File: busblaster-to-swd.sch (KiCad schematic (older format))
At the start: 5 parts, among them J101 CONN_02X10, J102 Tag Connect, J103 CONN_02X05

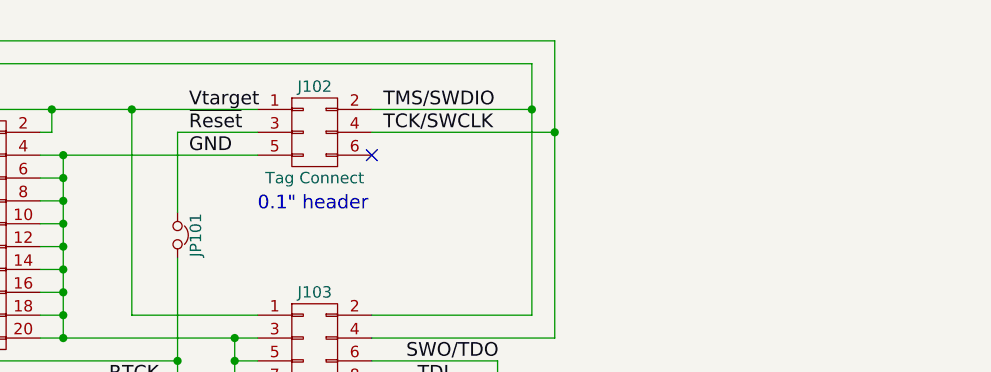
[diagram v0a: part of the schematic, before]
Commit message: Add SWCLK pullup resistor footprint
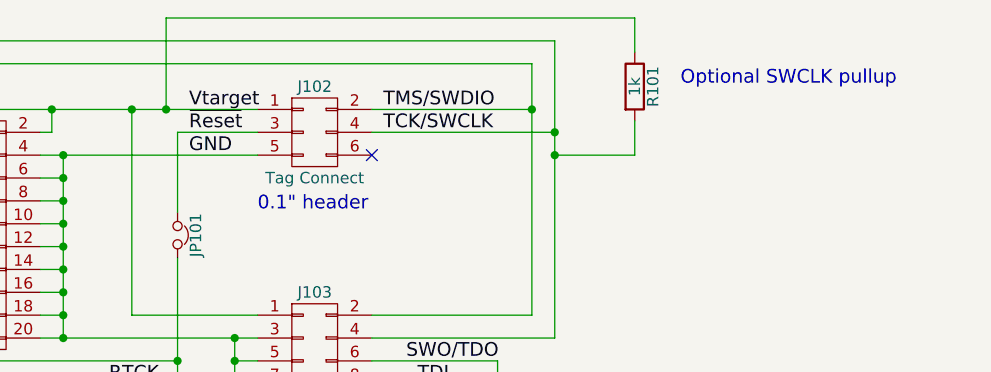
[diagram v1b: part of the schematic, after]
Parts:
- added R101: 1k, Resistors_SMD:R_0603_HandSoldering, symbol R
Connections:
- net TCK/SWCLK: now also R101.2
- net Vtarget: now also R101.1
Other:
- note added: "Optional SWCLK pullup"
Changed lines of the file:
@@
 LIBS:contrib
 LIBS:valves
+LIBS:busblaster-to-swd-cache
 EELAYER 25 0
 EELAYER END
@@
 Text Label 4200 3900 0    60   ~ 0
 RTCK
+$Comp
+L R R101
+U 1 1 590555B6
+P 6500 2600
+F 0 "R101" V 6580 2600 50  0000 C CNN
+F 1 "1k" V 6500 2600 50  0000 C CNN
+F 2 "Resistors_SMD:R_0603_HandSoldering" V 6430 2600 50  0001 C CNN
+F 3 "" H 6500 2600 50  0001 C CNN
+	1    6500 2600
+	1    0    0    -1
+$EndComp
+Wire Wire Line
+	6150 2900 6500 2900
+Wire Wire Line
+	6500 2900 6500 2750
+Connection ~ 6150 2900
+Wire Wire Line
+	6500 2450 6500 2300
+Wire Wire Line
+	6500 2300 4450 2300
+Wire Wire Line
+	4450 2300 4450 2700
+Connection ~ 4450 2700
+Text Notes 6700 2600 0    60   ~ 0
+Optional SWCLK pullup
 $EndSCHEMATC

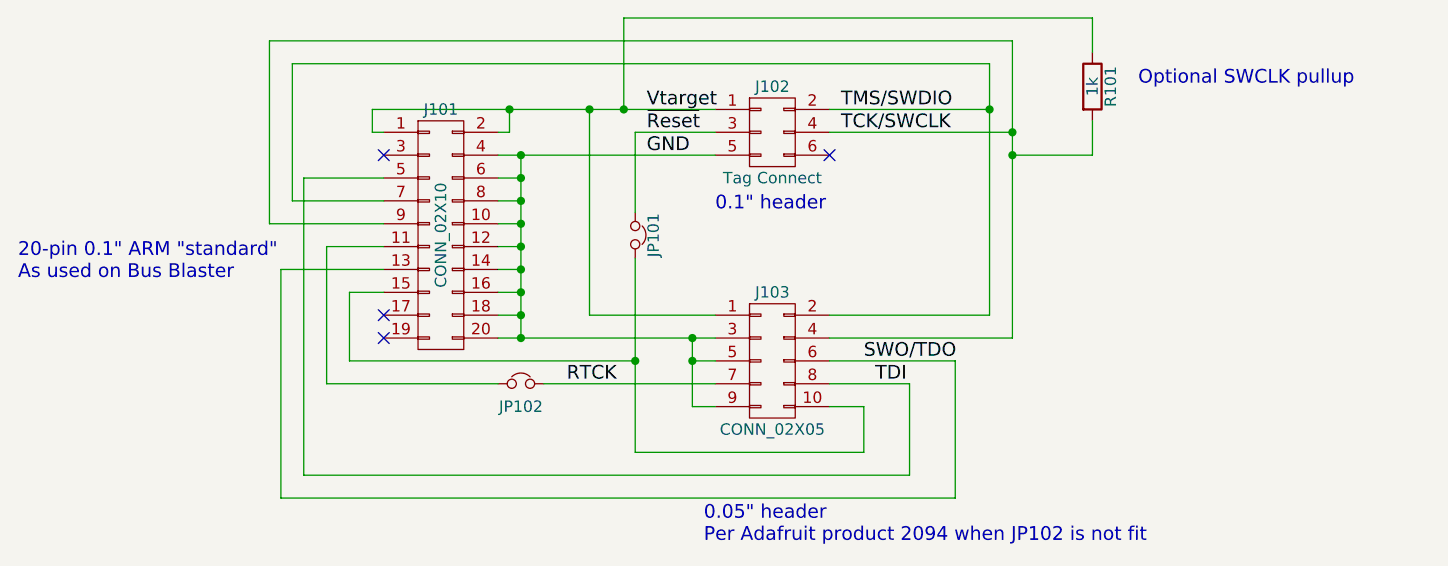
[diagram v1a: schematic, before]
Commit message: Connect SWO to Tag-Connect, move SWCLK pullup
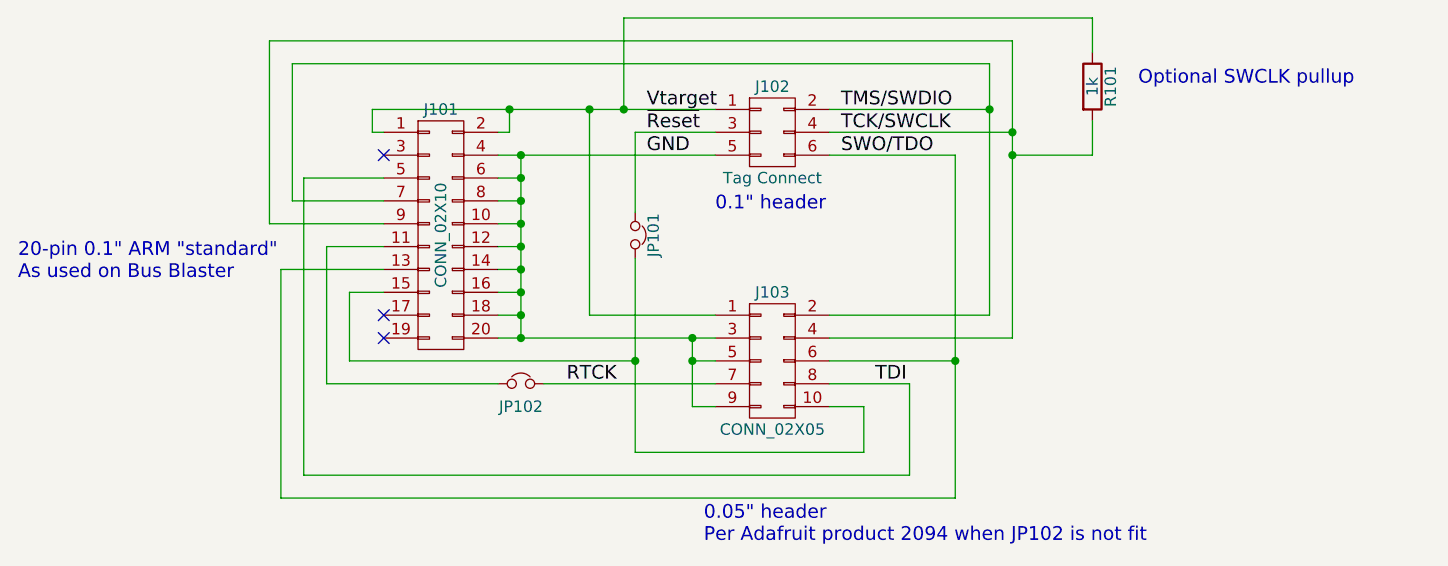
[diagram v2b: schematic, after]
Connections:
- net SWO/TDO: now also J102.6 (P6)
- no-connect marks 4 -> 3
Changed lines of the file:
@@
 Text Label 4550 2900 0    60   ~ 0
 GND
-NoConn ~ 5350 2900
 Text Label 5400 2700 0    60   ~ 0
 TMS/SWDIO
@@
 Wire Wire Line
 	6150 3700 5350 3700
-Text Label 5500 3800 0    60   ~ 0
+Text Label 5400 2900 0    60   ~ 0
 SWO/TDO
 Wire Wire Line
@@
 	2950 3400 2950 4400
 Wire Wire Line
-	2950 4400 5900 4400
-Wire Wire Line
-	5900 4400 5900 3800
+	5900 4400 2950 4400
+Wire Wire Line
+	5900 2900 5900 4400
 Wire Wire Line
 	5900 3800 5350 3800
@@
 Text Notes 6700 2600 0    60   ~ 0
 Optional SWCLK pullup
+Wire Wire Line
+	5350 2900 5900 2900
+Connection ~ 5900 3800
 $EndSCHEMATC
